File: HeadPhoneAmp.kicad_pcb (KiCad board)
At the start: 2 copper layers, 50 x 50 mm, 31 parts, among them J1 Conn_01x03_Male, J2 Conn_01x03_Male, J3 Conn_01x02_Male, J4 Conn_01x02_Male, SW1 SW_DPST_x2, U1 OPA2134, U2 TPA6120A2_HSOP20

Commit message: Add PCB
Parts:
- removed J1, J2: Conn_01x03_Male, Connector_PinHeader_2.54mm:PinHeader_1x03_P2.54mm_Vertical
- removed J3, J4: Conn_01x02_Male, Connector_PinHeader_2.54mm:PinHeader_1x02_P2.54mm_Vertical
- removed SW1: SW_DPST_x2, Connector_PinHeader_2.54mm:PinHeader_2x02_P2.54mm_Vertical
- added +9V: SolderWirePad_1x01_Drill0.8mm, Connector_Wire:SolderWirePad_1x01_Drill0.8mm, F.Cu at (145.9, 116.3)
- added -9V: SolderWirePad_1x01_Drill0.8mm, Connector_Wire:SolderWirePad_1x01_Drill0.8mm, F.Cu at (145.9, 133.8)
- added GND: SolderWirePad_1x01_Drill0.8mm, Connector_Wire:SolderWirePad_1x01_Drill0.8mm, F.Cu at (102.3, 125.1)
- added INL: SolderWirePad_1x01_Drill0.8mm, Connector_Wire:SolderWirePad_1x01_Drill0.8mm, F.Cu at (102.9, 131.7)
- added INR: SolderWirePad_1x01_Drill0.8mm, Connector_Wire:SolderWirePad_1x01_Drill0.8mm, F.Cu at (102.8, 118.2)
- added OUTL: SolderWirePad_1x01_Drill0.8mm, Connector_Wire:SolderWirePad_1x01_Drill0.8mm, F.Cu at (124.5, 146.4)
- added OUTR: SolderWirePad_1x01_Drill0.8mm, Connector_Wire:SolderWirePad_1x01_Drill0.8mm, F.Cu at (125.2, 104.3)
- C10, C5, C6, C7, C8, C9: footprint Capacitor_THT:C_Rect_L4.0mm_W2.5mm_P2.50mm -> Capacitor_THT:C_Rect_L7.2mm_W2.5mm_P5.00mm_FKS2_FKP2_MKS2_MKP2
- moved C7 16.6 mm to (137.3, 132.4), turned to 180 degrees
- moved R11 12.4 mm to (102.8, 114.9), turned to 90 degrees
- moved R12 12.1 mm to (109.6, 114.9), turned to 90 degrees
- moved R1 11.5 mm to (131.1, 146.4), turned to 90 degrees
- moved C5 11.4 mm to (137.3, 117.5), turned to 180 degrees
- moved R9 11.4 mm to (134.9, 114.4), turned to 90 degrees
- moved R6 10.4 mm to (109.4, 134.8), turned to 270 degrees
- moved R5 10.2 mm to (102.8, 134.8), turned to 270 degrees
- moved R10 9.34 mm to (128.4, 104.3), turned to 270 degrees
- moved R7 8.94 mm to (131.6, 104.2), turned to 270 degrees
- moved R3 8.81 mm to (134.5, 136.2), turned to 270 degrees
- moved C10 6.89 mm to (127.0, 126.7), turned to 270 degrees
- moved C6 6.71 mm to (120.5, 122.5), turned to 270 degrees
- moved C9 6.65 mm to (127.1, 123.3)
- moved C1 5.00 mm to (106.0, 140.0)
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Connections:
- net Net-(C1-Pad2) renamed /INL
- net Net-(C3-Pad2) renamed /INR
- R10 pad 1: Net-(J1-Pad3) -> /OUTR
- R4 pad 1: Net-(J1-Pad1) -> /OUTL
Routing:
- net -9V: track 0.00 -> 67.8 mm
- net +9V: track 0.00 -> 59.1 mm
- net Net-(R3-Pad2): track 0.00 -> 30.8 mm
- net Net-(R9-Pad2): track 0.00 -> 27.4 mm
- net Net-(R1-Pad1): track 0.00 -> 19.4 mm
- net Net-(R10-Pad2): track 0.00 -> 19.1 mm
- net Net-(C1-Pad1): track 0.00 -> 15.7 mm
- net Net-(C3-Pad1): track 0.00 -> 15.4 mm
- net Net-(C2-Pad2): track 0.00 -> 11.4 mm
- net Net-(R1-Pad2): track 0.00 -> 10.0 mm
- net Net-(C4-Pad2): track 0.00 -> 9.95 mm
- net Net-(R7-Pad2): track 0.00 -> 9.18 mm
- net /INR: track 0.00 -> 6.60 mm
- net /INL: track 0.00 -> 6.42 mm
- net /OUTL: track 0.00 -> 3.36 mm
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- added copper zone on B.Cu, net GND
- added copper zone on F.Cu, net GND
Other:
- net class Default: trace_width 0.25 -> 0.3
- net class Power added: clearance 0.2, trace_width 1, via_dia 0.8, via_drill 0.4

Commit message: Add GND to PCB power
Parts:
- added GND: SolderWirePad_1x01_Drill0.8mm, Connector_Wire:SolderWirePad_1x01_Drill0.8mm, F.Cu at (146.0, 127.7)
- added GND: SolderWirePad_1x01_Drill0.8mm, Connector_Wire:SolderWirePad_1x01_Drill0.8mm, F.Cu at (146.0, 122.1)
- turned +9V to 90 degrees
- turned -9V to 270 degrees
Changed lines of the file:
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@@
     (tracks 113)
     (zones 0)
-    (modules 33)
+    (modules 35)
     (nets 18)
   )
   (page A4)
   (layers
-    (0 F.Cu signal hide)
+    (0 F.Cu signal)
     (31 B.Cu signal)
     (32 B.Adhes user)
@@
   )
   (module Connector_Wire:SolderWirePad_1x01_Drill0.8mm (layer F.Cu)
-    (at 145.9 133.8)
+    (at 146 127.7 270)
     (descr "Wire solder connection")
     (tags connector)
     (attr virtual)
-    (fp_text reference -9V (at 0 -2.54) (layer F.SilkS)
-      (effects (font (size 1 1) (thickness 0.15)))
-    )
-    (fp_text value SolderWirePad_1x01_Drill0.8mm (at 0 2.54) (layer F.Fab) hide
+    (fp_text reference GND (at 0 -2.54 90) (layer F.SilkS)
+      (effects (font (size 1 1) (thickness 0.15)))
+    )
+    (fp_text value SolderWirePad_1x01_Drill0.8mm (at 0 2.54 90) (layer F.Fab) hide
+      (effects (font (size 1 1) (thickness 0.15)))
+    )
+    (fp_text user %R (at 0 0 90) (layer F.Fab) hide
+      (effects (font (size 1 1) (thickness 0.15)))
+    )
+    (fp_line (start -1.5 -1.5) (end 1.5 -1.5) (layer F.CrtYd) (width 0.05))
+    (fp_line (start -1.5 -1.5) (end -1.5 1.5) (layer F.CrtYd) (width 0.05))
+    (fp_line (start 1.5 1.5) (end 1.5 -1.5) (layer F.CrtYd) (width 0.05))
+    (fp_line (start 1.5 1.5) (end -1.5 1.5) (layer F.CrtYd) (width 0.05))
+    (pad 1 thru_hole circle (at 0 0 270) (size 1.99898 1.99898) (drill 0.8001) (layers *.Cu *.Mask)
+      (net 3 GND))
+  )
+  (module Connector_Wire:SolderWirePad_1x01_Drill0.8mm (layer F.Cu)
+    (at 146 122.1 270)
+    (descr "Wire solder connection")
+    (tags connector)
+    (attr virtual)
+    (fp_text reference GND (at 0 -2.54 90) (layer F.SilkS)
+      (effects (font (size 1 1) (thickness 0.15)))
+    )
+    (fp_text value SolderWirePad_1x01_Drill0.8mm (at 0 2.54 90) (layer F.Fab) hide
       (effects (font (size 1 1) (thickness 0.15)))
     )
@@
     (fp_line (start -1.5 -1.5) (end -1.5 1.5) (layer F.CrtYd) (width 0.05))
     (fp_line (start -1.5 -1.5) (end 1.5 -1.5) (layer F.CrtYd) (width 0.05))
-    (fp_text user %R (at 0 0) (layer F.Fab) hide
-      (effects (font (size 1 1) (thickness 0.15)))
-    )
-    (pad 1 thru_hole circle (at 0 0) (size 1.99898 1.99898) (drill 0.8001) (layers *.Cu *.Mask)
-      (net 7 -9V))
+    (fp_text user %R (at 0 0 90) (layer F.Fab) hide
+      (effects (font (size 1 1) (thickness 0.15)))
+    )
+    (pad 1 thru_hole circle (at 0 0 270) (size 1.99898 1.99898) (drill 0.8001) (layers *.Cu *.Mask)
+      (net 3 GND))
   )
   (module Connector_Wire:SolderWirePad_1x01_Drill0.8mm (layer F.Cu)
-    (at 145.9 116.3)
+    (at 145.9 133.8 270)
     (descr "Wire solder connection")
     (tags connector)
     (attr virtual)
-    (fp_text reference +9V (at -0.3 2.6) (layer F.SilkS)
-      (effects (font (size 1 1) (thickness 0.15)))
-    )
-    (fp_text value SolderWirePad_1x01_Drill0.8mm (at 0 2.54) (layer F.Fab) hide
+    (fp_text reference -9V (at 0 -2.54 90) (layer F.SilkS)
+      (effects (font (size 1 1) (thickness 0.15)))
+    )
+    (fp_text value SolderWirePad_1x01_Drill0.8mm (at 0 2.54 90) (layer F.Fab) hide
       (effects (font (size 1 1) (thickness 0.15)))
     )
@@
     (fp_line (start -1.5 -1.5) (end -1.5 1.5) (layer F.CrtYd) (width 0.05))
     (fp_line (start -1.5 -1.5) (end 1.5 -1.5) (layer F.CrtYd) (width 0.05))
-    (fp_text user %R (at 0 0) (layer F.Fab) hide
-      (effects (font (size 1 1) (thickness 0.15)))
-    )
-    (pad 1 thru_hole circle (at 0 0) (size 1.99898 1.99898) (drill 0.8001) (layers *.Cu *.Mask)
+    (fp_text user %R (at 0 0 90) (layer F.Fab) hide
+      (effects (font (size 1 1) (thickness 0.15)))
+    )
+    (pad 1 thru_hole circle (at 0 0 270) (size 1.99898 1.99898) (drill 0.8001) (layers *.Cu *.Mask)
+      (net 7 -9V))
+  )
+  (module Connector_Wire:SolderWirePad_1x01_Drill0.8mm (layer F.Cu)
+    (at 145.9 116.3 90)
+    (descr "Wire solder connection")
+    (tags connector)
+    (attr virtual)
+    (fp_text reference +9V (at -0.3 2.6 90) (layer F.SilkS)
+      (effects (font (size 1 1) (thickness 0.15)))
+    )
+    (fp_text value SolderWirePad_1x01_Drill0.8mm (at 0 2.54 90) (layer F.Fab) hide
+      (effects (font (size 1 1) (thickness 0.15)))
+    )
+    (fp_line (start 1.5 1.5) (end -1.5 1.5) (layer F.CrtYd) (width 0.05))
+    (fp_line (start 1.5 1.5) (end 1.5 -1.5) (layer F.CrtYd) (width 0.05))
+    (fp_line (start -1.5 -1.5) (end -1.5 1.5) (layer F.CrtYd) (width 0.05))
+    (fp_line (start -1.5 -1.5) (end 1.5 -1.5) (layer F.CrtYd) (width 0.05))
+    (fp_text user %R (at 0 0 90) (layer F.Fab) hide
+      (effects (font (size 1 1) (thickness 0.15)))
+    )
+    (pad 1 thru_hole circle (at 0 0 90) (size 1.99898 1.99898) (drill 0.8001) (layers *.Cu *.Mask)
       (net 6 +9V))
   )
@@
   (segment (start 114.46 129.75137) (end 123.2 138.49137) (width 0.3) (layer B.Cu) (net 10))
   (segment (start 114.46 128.62) (end 114.46 129.75137) (width 0.3) (layer B.Cu) (net 10))
-  (segment (start 127.74 146.4) (end 127.7 146.36) (width 0.3) (layer F.Cu) (net 16))
   (segment (start 134.865 114.435) (end 134.9 114.4) (width 0.3) (layer F.Cu) (net 11))
   (segment (start 134.865 120.25) (end 134.865 114.435) (width 0.3) (layer F.Cu) (net 11))
@@
   (segment (start 102.8 116.03137) (end 102.8 118.2) (width 0.3) (layer F.Cu) (net 15))
   (segment (start 102.8 114.9) (end 102.8 116.03137) (width 0.3) (layer F.Cu) (net 15))
+  (segment (start 127.74 146.4) (end 127.7 146.36) (width 0.3) (layer F.Cu) (net 16))
   (segment (start 126.66863 146.4) (end 124.5 146.4) (width 0.3) (layer F.Cu) (net 16))
   (segment (start 127.8 146.4) (end 126.66863 146.4) (width 0.3) (layer F.Cu) (net 16))

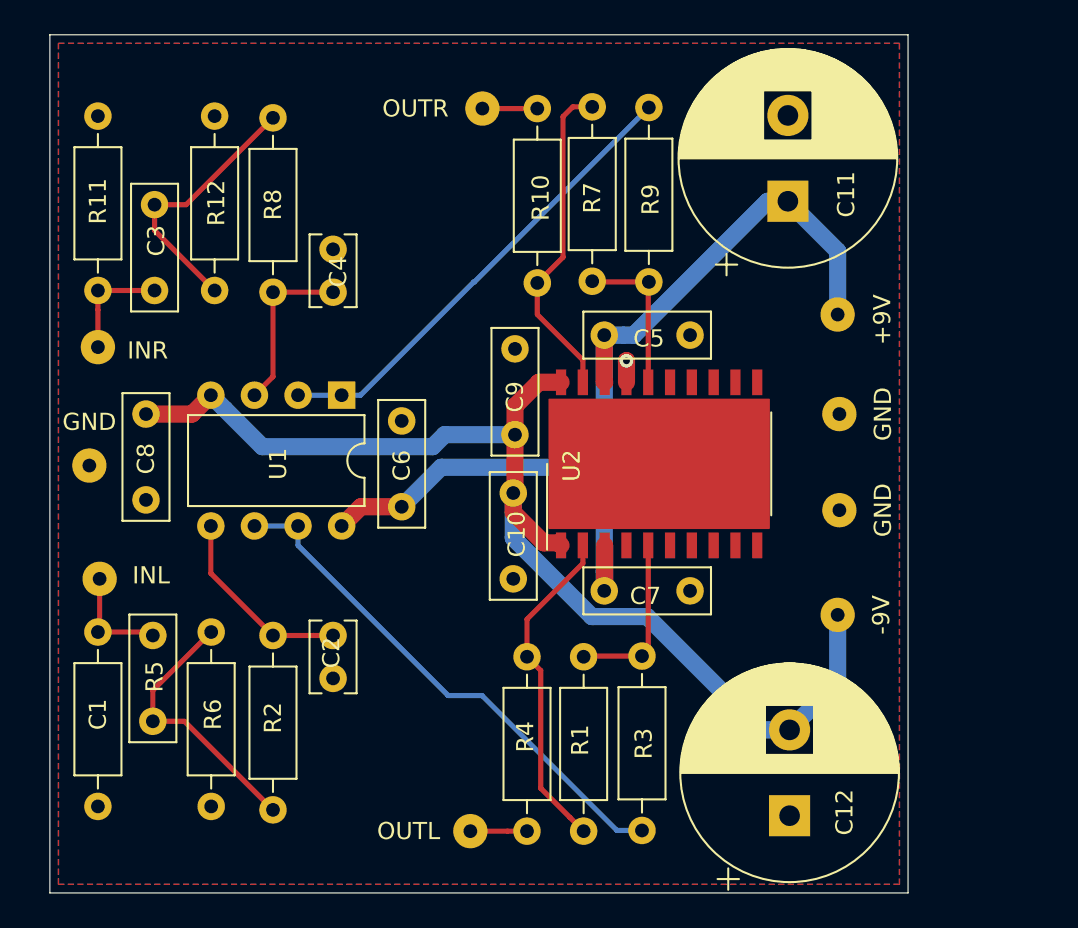
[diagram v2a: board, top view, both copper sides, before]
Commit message: Bump to KiCad 6
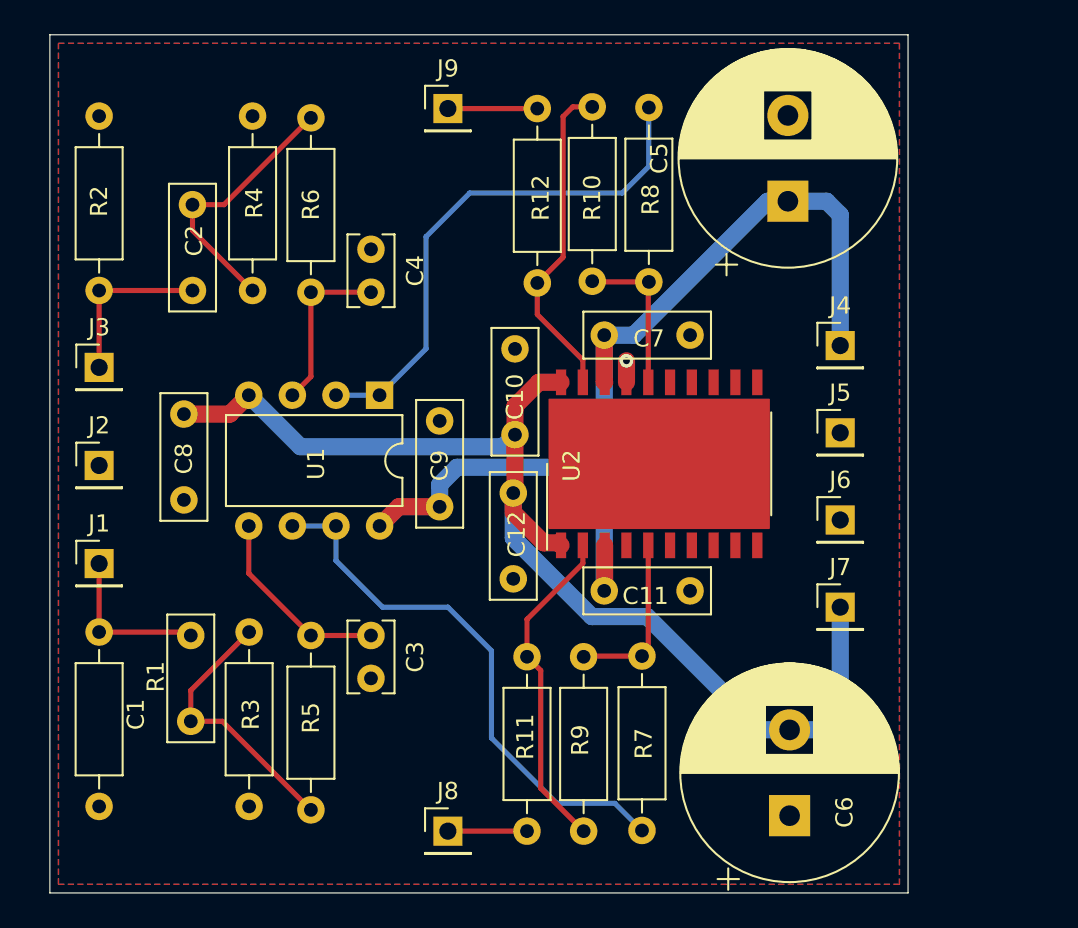
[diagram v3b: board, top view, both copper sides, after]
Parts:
- removed +9V, -9V, GND (x3), INL, INR, OUTL, OUTR: SolderWirePad_1x01_Drill0.8mm, Connector_Wire:SolderWirePad_1x01_Drill0.8mm
- added J1: Conn_01x01_Male, Connector_PinHeader_2.54mm:PinHeader_1x01_P2.54mm_Vertical, F.Cu at (102.9, 130.8)
- added J2: Conn_01x01_Male, Connector_PinHeader_2.54mm:PinHeader_1x01_P2.54mm_Vertical, F.Cu at (102.9, 125.1)
- added J3: Conn_01x01_Male, Connector_PinHeader_2.54mm:PinHeader_1x01_P2.54mm_Vertical, F.Cu at (102.9, 119.4)
- added J4: Conn_01x01_Male, Connector_PinHeader_2.54mm:PinHeader_1x01_P2.54mm_Vertical, F.Cu at (146.1, 118.1)
- added J5: Conn_01x01_Male, Connector_PinHeader_2.54mm:PinHeader_1x01_P2.54mm_Vertical, F.Cu at (146.1, 123.2)
- added J6: Conn_01x01_Male, Connector_PinHeader_2.54mm:PinHeader_1x01_P2.54mm_Vertical, F.Cu at (146.1, 128.3)
- added J7: Conn_01x01_Male, Connector_PinHeader_2.54mm:PinHeader_1x01_P2.54mm_Vertical, F.Cu at (146.1, 133.3)
- added J8: Conn_01x01_Male, Connector_PinHeader_2.54mm:PinHeader_1x01_P2.54mm_Vertical, F.Cu at (123.2, 146.4)
- added J9: Conn_01x01_Male, Connector_PinHeader_2.54mm:PinHeader_1x01_P2.54mm_Vertical, F.Cu at (123.2, 104.3)
- moved C2 2.21 mm to (108.3, 109.9)
- moved C8 2.21 mm to (107.8, 122.1)
- moved R4 2.21 mm to (111.8, 114.9)
- moved C1 2.21 mm to (108.2, 140.0)
- moved C3 2.21 mm to (118.7, 137.5)
- moved C4 2.21 mm to (118.7, 112.5)
- moved C9 2.21 mm to (122.7, 122.5)
- moved R3 2.21 mm to (111.6, 134.8)
- moved R5 2.21 mm to (115.2, 135.0)
- moved R6 2.21 mm to (115.2, 115.0)
- moved U1 2.21 mm to (119.2, 121.0)
- moved R1 0.07 mm to (102.9, 134.8)
- moved R2 0.07 mm to (102.9, 114.9)
- renumbered C9 to C10, C7 to C11, C10 to C12, C3 to C2, C2 to C3, C11 to C5, C12 to C6, C5 to C7, C6 to C9, R5 to R1, R7 to R10, R4 to R11, R10 to R12, R11 to R2, R6 to R3, R12 to R4, R2 to R5, R8 to R6, R3 to R7, R9 to R8, R1 to R9
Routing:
- net Net-(R8-Pad2): track 27.4 -> 31.0 mm
- net /INR: track 6.60 -> 10.0 mm
- net /INL: track 6.42 -> 9.41 mm
- net /OUTR: track 3.20 -> 5.21 mm
- net +9V: track 59.1 -> 60.9 mm
- net /OUTL: track 3.36 -> 4.61 mm
- net Net-(R7-Pad2): track 30.8 -> 31.9 mm
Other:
- net class Default removed
- net class Power removed
